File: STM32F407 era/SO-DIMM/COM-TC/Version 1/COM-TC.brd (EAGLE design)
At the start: 127 x 165.1 mm, 113 parts, among them J1 CON1, J2 CON1, J3 SO-DIMM-CPU, J4 FTDI_DEVICE, Q4 PMV20XNE, U1 IRF9332PBF, U10 SN65HVD232D, U11 MAX9926, U12 MCP6004-E/SL, U13 MCP6004-E/SL, U14 MCP6004-E/SL, U17 MC74AC573DWG, U18 MC74AC573DWG, U19 MC74AC573DWG, U2 5V, U20 MC74AC573DWG, U3 TPS54331D, U4 3,3V, U5 MAX9926, U6 MCP6004-E/SL, X1 057-014-1

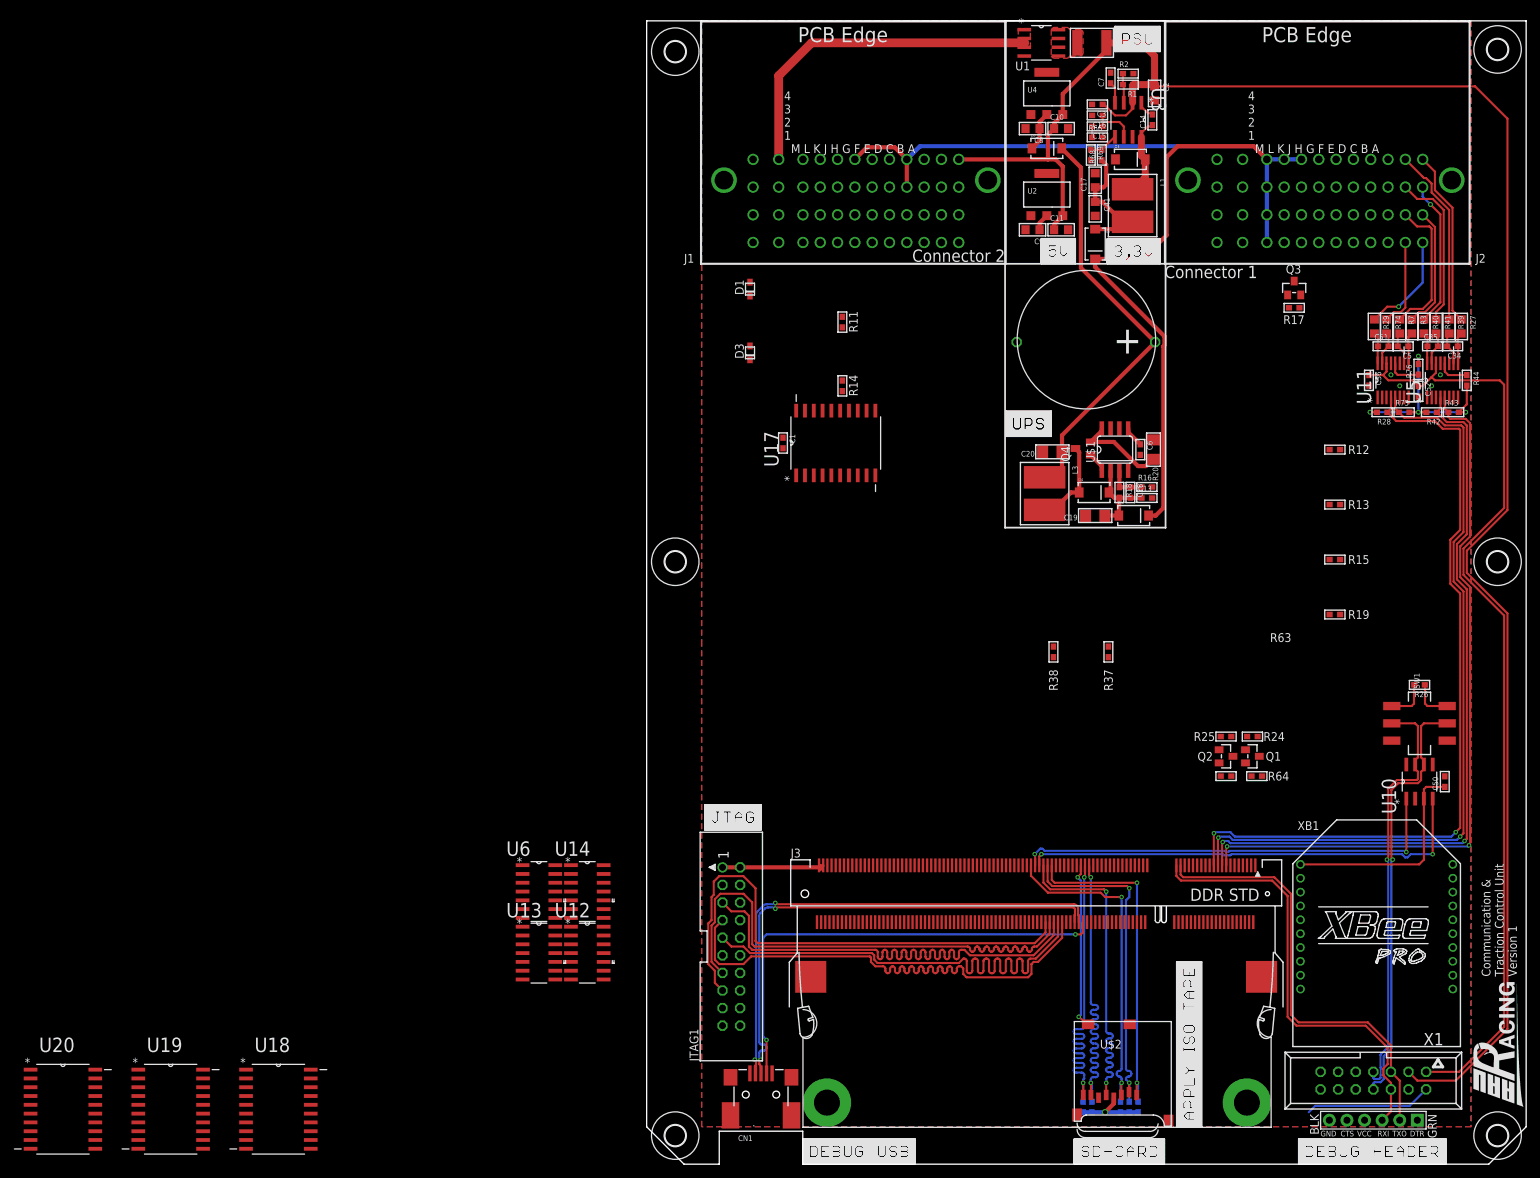
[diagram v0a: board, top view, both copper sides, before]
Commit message: USB to UART done, mork work on COM/TC
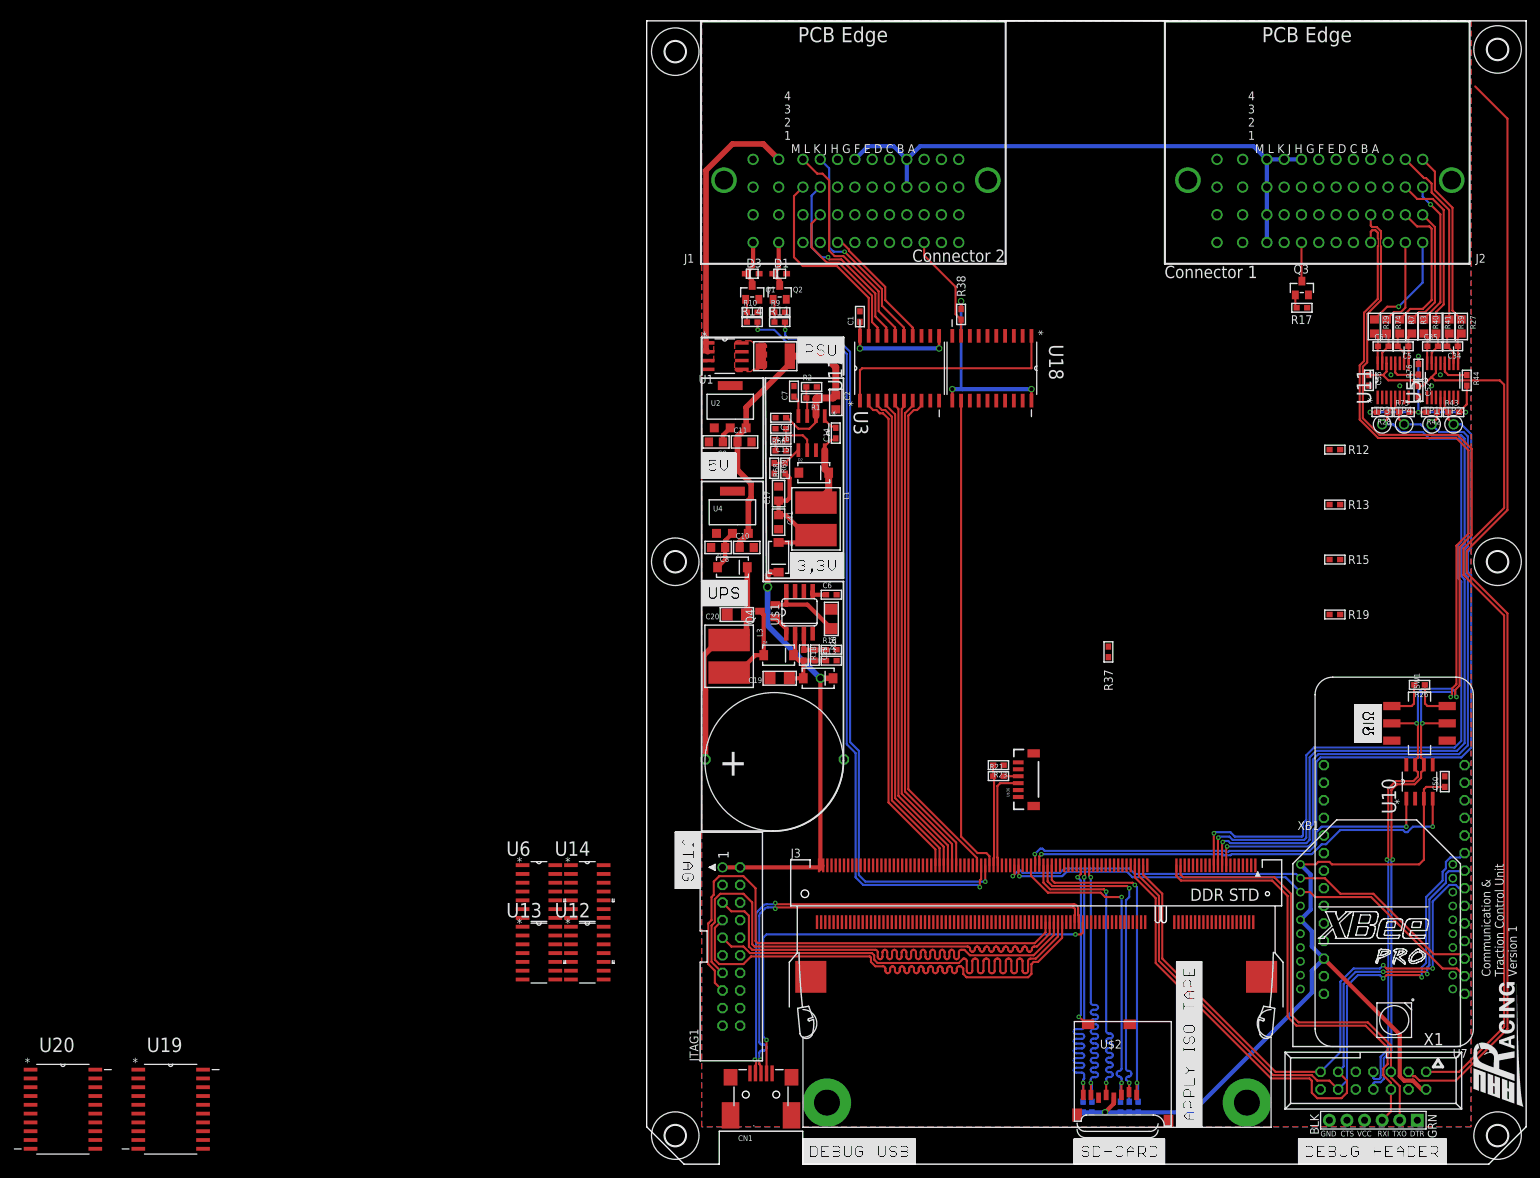
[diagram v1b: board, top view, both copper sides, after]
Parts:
- removed R24, R25, R63, R64: 500, microbuilder:_0603
- added R10, R9: 500, microbuilder:_0603
- added R21: 499, microbuilder:_0603
- added R23: 976, microbuilder:_0603
- added TP1, TP2, TP3, TP4: TEST_POINT_0.040IN, headers:TESTPOINT_0.040IN
- added U$36: EM406, SparkFun:EM406
- added U7: LoPy, AAU-Racing:LOPY
- R11, R14: value 120 -> 220
- moved U18 148.5 mm to (49.8, 114.9), turned to 270 degrees
- moved Q1 98.5 mm to (15.2, 125.9), turned to 0 degrees
- moved Q2 93.0 mm to (19.2, 125.9), turned to 0 degrees
- moved C4 75.8 mm to (18.4, 58.1), turned to 0 degrees
- moved D7 75.6 mm to (12.4, 86.2)
- moved U4 75.6 mm to (12.4, 94.1)
- moved C10 75.6 mm to (14.4, 89.1)
- moved C8 75.6 mm to (10.3, 89.1)
- moved C15 64.3 mm to (19.4, 104.6)
- moved C41 64.3 mm to (19.1, 92.7)
- moved C14 64.3 mm to (27.3, 105.6)
- moved C16 64.3 mm to (19.4, 106.2)
- moved C17 64.3 mm to (19.1, 96.8)
- moved C3 64.3 mm to (19.4, 107.8)
- moved C7 64.3 mm to (21.3, 111.6)
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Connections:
- removed net COMRX: J3.67
- removed net COMTX: J3.65
- removed net ECU1L: Q1.2
- removed net ECU2L: Q2.2
- removed net GND-RELAY: D1.A, D3.A
- removed net N$34: Q1.1, R24.2
- removed net N$35: Q2.1, R25.2
- removed net RS232RX: J2.C1
- removed net RS232TX: J2.C2
- new net COM_RX: J2.C1, J3.67
- new net COM_TX: J2.C2, J3.65
- new net GPS_RX: J3.115, R21.1, R23.2
- new net GPS_TX: J3.113, U$36.3
- new net RXD1: R21.2, U$36.4
- net 3.3V: now also U18.11, U18.20, U7.3,3V, XB1.5; no longer R24.1, R25.1
- net 5.0V: now also U$36.2, U7.5V; no longer R63.1, R64.1
- net DIG_IO_EN: now also U18.1
- net ECU1: no longer Q1.3, R64.2
- net ECU2: no longer Q2.3, R63.2
- net GND: now also D1.A, D3.A, Q1.2, Q2.2, R10.2, R23.1, R9.2, U$36.1, U$36.5, U18.10, U7.GND
- net MISO: now also J3.45, U7.38
- net MOSI: now also J3.47, U7.16
- net N$10: now also Q1.1, R10.1
- net N$6: now also Q2.1, R9.1
- net OC1: now also J3.119
- net OC2: now also J3.121
- net OILP: now also R38.2, U18.9
- net OILPI: now also J3.117, U18.12; no longer R38.2
- net RLY1: now also Q2.3
- net RLY2: now also Q1.3
- net RPM1: now also TP1.TESTPOINT
- net RPM2: now also TP2.TESTPOINT
- net RPM3: now also TP3.TESTPOINT
- net RPM4: now also TP4.TESTPOINT
- net SCK: now also J3.43, U7.34
- net TELE_RX: now also U7.41, XB1.2
- net TELE_TX: now also U7.40, XB1.3
- net VCC: no longer U18.20
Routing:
- net OC2: track 0.00 -> 113.3 mm, vias 0 -> 2
- net OC1: track 0.00 -> 109.4 mm, vias 0 -> 2
- net MOSI: track 0.00 -> 100.4 mm, vias 0 -> 2
- net CAN_P: track 61.6 -> 159.1 mm, vias 1 -> 3
- net MISO: track 0.00 -> 97.3 mm, vias 0 -> 2
- net CAN_N: track 62.5 -> 157.5 mm, vias 1 -> 3
- net SCK: track 0.00 -> 88.4 mm, vias 0 -> 2
- net TELE_RX: track 0.00 -> 73.0 mm, vias 0 -> 1
- net TELE_TX: track 0.00 -> 72.4 mm, vias 0 -> 1
- net BITEL: track 0.00 -> 72.3 mm
- net HB2-DIRA: track 0.00 -> 71.7 mm
- net HB2-PWM: track 0.00 -> 71.1 mm
- net HB1-DIRA: track 0.00 -> 70.6 mm
- net HB1-PWM: track 0.00 -> 70.5 mm
- net HB2-DIRB: track 0.00 -> 70.3 mm
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
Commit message: LoPy / Xbee telemtry receiver hybrid done
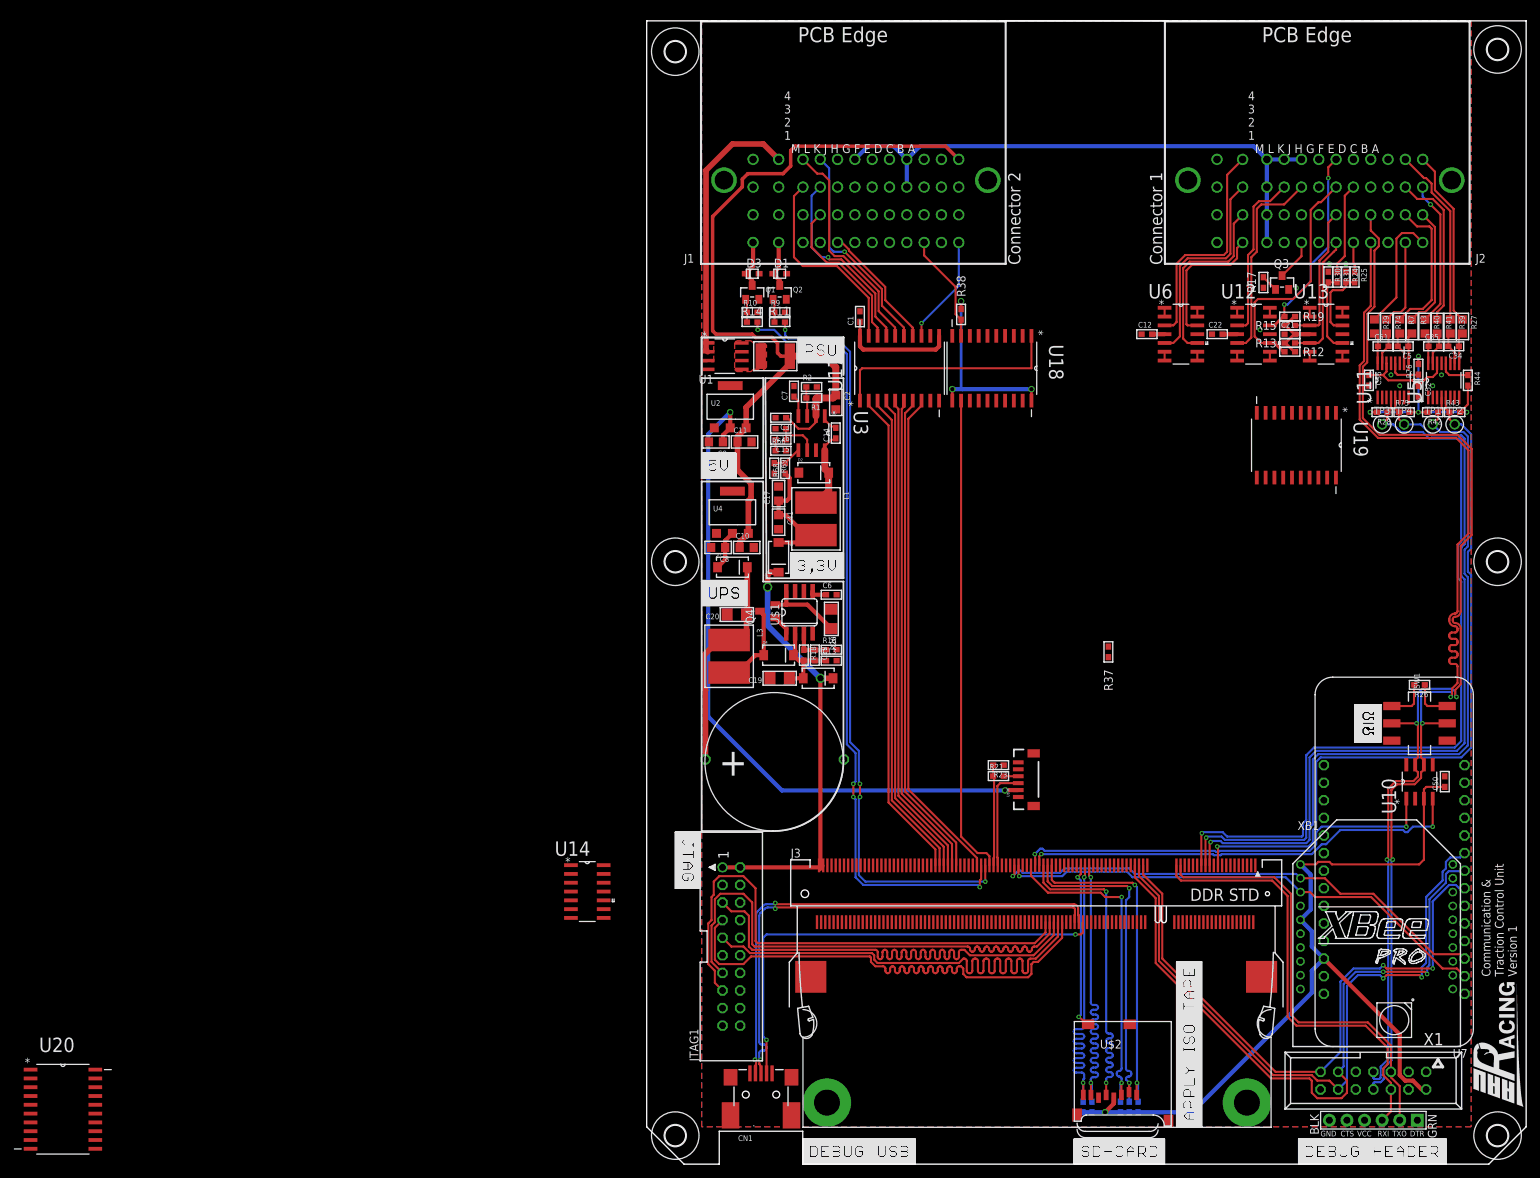
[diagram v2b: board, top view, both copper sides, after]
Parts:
- added C12, C21, C22: 100n, microbuilder:_0603
- added R24, R30: 976, microbuilder:_0603
- added R25, R31: 499, microbuilder:_0603
- moved U19 188.7 mm to (93.8, 103.8), turned to 270 degrees
- moved U13 144.6 mm to (98.1, 119.9)
- moved U12 131.3 mm to (87.6, 119.9)
- moved U6 122.8 mm to (77.2, 119.9)
- moved R19 43.5 mm to (92.9, 122.4)
- moved R15 34.4 mm to (92.9, 121.1), turned to 0 degrees
- moved R13 24.2 mm to (92.9, 118.6), turned to 0 degrees
- moved R12 15.6 mm to (92.9, 117.3)
- moved R17 6.65 mm to (89.1, 127.3), turned to 270 degrees
- moved Q3 2.97 mm to (91.8, 127.3)
- moved C35 0.16 mm to (113.7, 118.1)
- moved R43 0.16 mm to (116.7, 108.6)
- moved R44 0.16 mm to (118.6, 113.2)
- moved TP2 0.16 mm to (116.7, 106.8)
- moved C34 0.16 mm to (116.5, 118.1)
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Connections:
- new net CURRENT1B: J3.15, U13.13, U13.14
- new net CURRENT1H: J2.E1, R25.1
- new net CURRENT1L: R24.2, R25.2, U13.12
- new net CURRENT2B: J3.17, U13.8, U13.9
- new net CURRENT2H: J2.E3, R31.1
- new net CURRENT2L: R30.2, R31.2, U13.10
- net 3.3V: now also C12.2, C21.2, C22.2
- net BRAKEP: now also U12.12
- net BRAKEP2: now also U13.3
- net BRAKEP2B: now also U13.1, U13.2
- net BRAKEPB: now also U12.13, U12.14
- net GEARPOSAN: now also U12.5
- net GEARPOSANB: now also U12.6, U12.7
- net GND: now also C12.1, C21.1, C22.1, R24.1, R30.1, U12.11, U13.11, U6.11
- net RPM1: now also J3.23; no longer J3.17
- net RPM2: now also J3.19; no longer J3.15
- net RPM3: now also J3.27; no longer J3.21
- net RPM4: now also J3.25; no longer J3.19
- net SPEED: now also U12.3
- net SPEEDB: now also U12.1, U12.2
- net TRAVEL1: now also U6.5
- net TRAVEL1B: now also U6.6, U6.7
- net TRAVEL2: now also U6.3
- net TRAVEL2B: now also U6.1, U6.2
- net TRAVEL3: now also U6.10
- net TRAVEL3B: now also U6.8, U6.9
- net TRAVEL4: now also U6.12
- net TRAVEL4B: now also U6.13, U6.14
- net VTEMP: now also U13.5
- net VTEMP2: now also U12.10
- net VTEMP2B: now also U12.8, U12.9
- net VTEMPB: now also U13.6, U13.7
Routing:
- net 12V: track 216.2 -> 127.9 mm
- net VTEMP2: track 0.00 -> 34.9 mm
- net TRAVEL2: track 0.00 -> 32.6 mm
- net TRAVEL1: track 0.00 -> 31.2 mm
- net GEARPOSAN: track 0.00 -> 29.0 mm
- net BRAKEP: track 0.00 -> 28.7 mm, vias 0 -> 2
- net TRAVEL3: track 0.00 -> 27.0 mm
- net 5.0V: track 156.7 -> 130.9 mm
- net SPEED: track 0.00 -> 24.5 mm
- net BRAKEP2: track 0.00 -> 20.4 mm
- net TRAVEL4: track 0.00 -> 20.1 mm
- net VTEMP: track 0.00 -> 18.9 mm
- net BITE: track 0.00 -> 15.7 mm, vias 0 -> 1
- net 3.3V: track 332.2 -> 346.3 mm
- net CURRENT2H: track 0.00 -> 13.2 mm
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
